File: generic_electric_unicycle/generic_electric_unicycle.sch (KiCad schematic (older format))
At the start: 2 parts

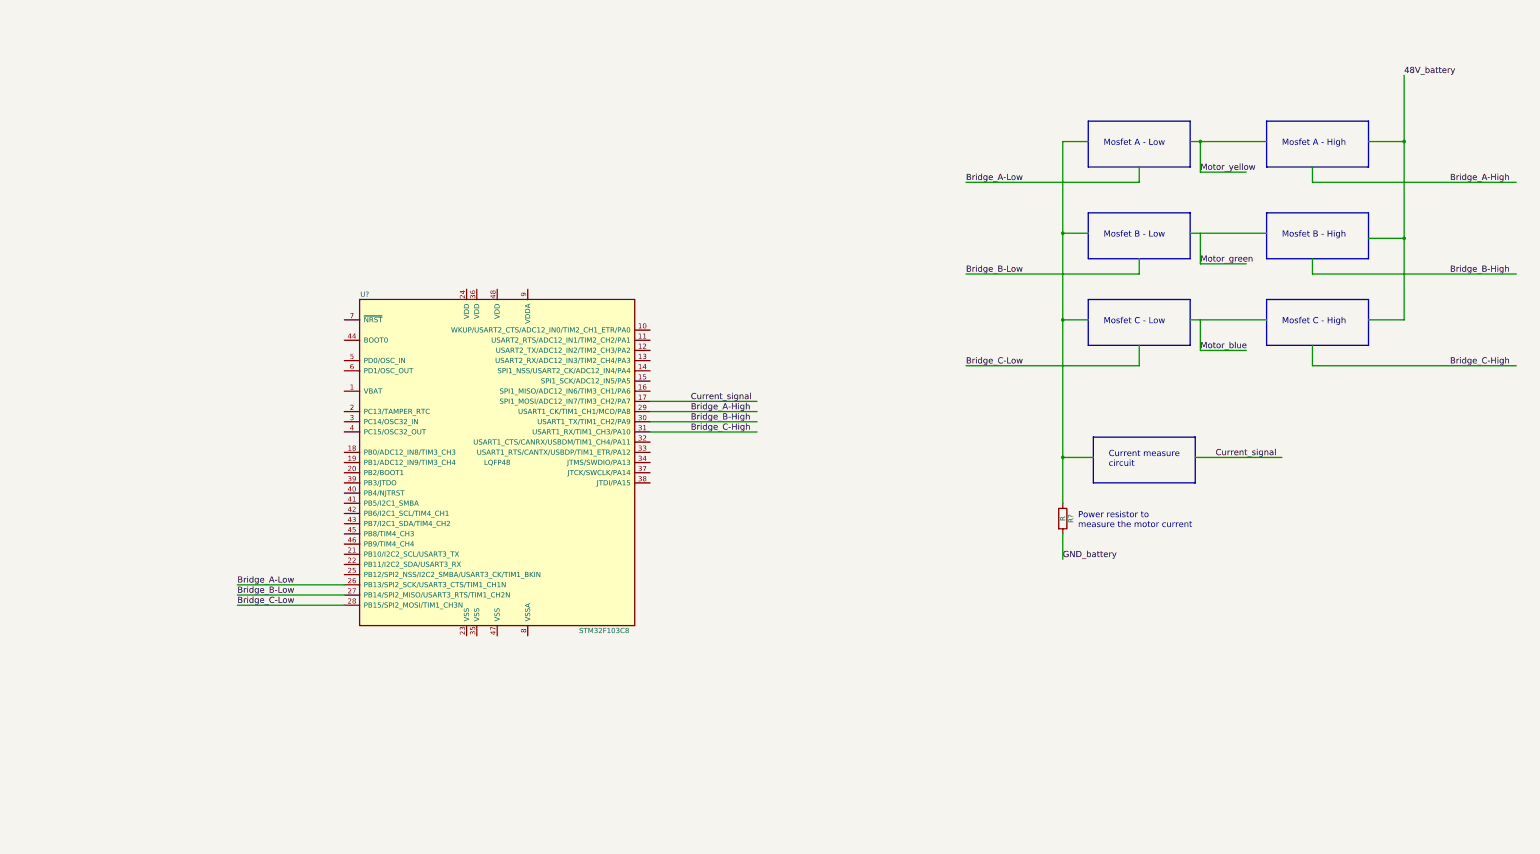
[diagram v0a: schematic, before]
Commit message: Added the hall sensors
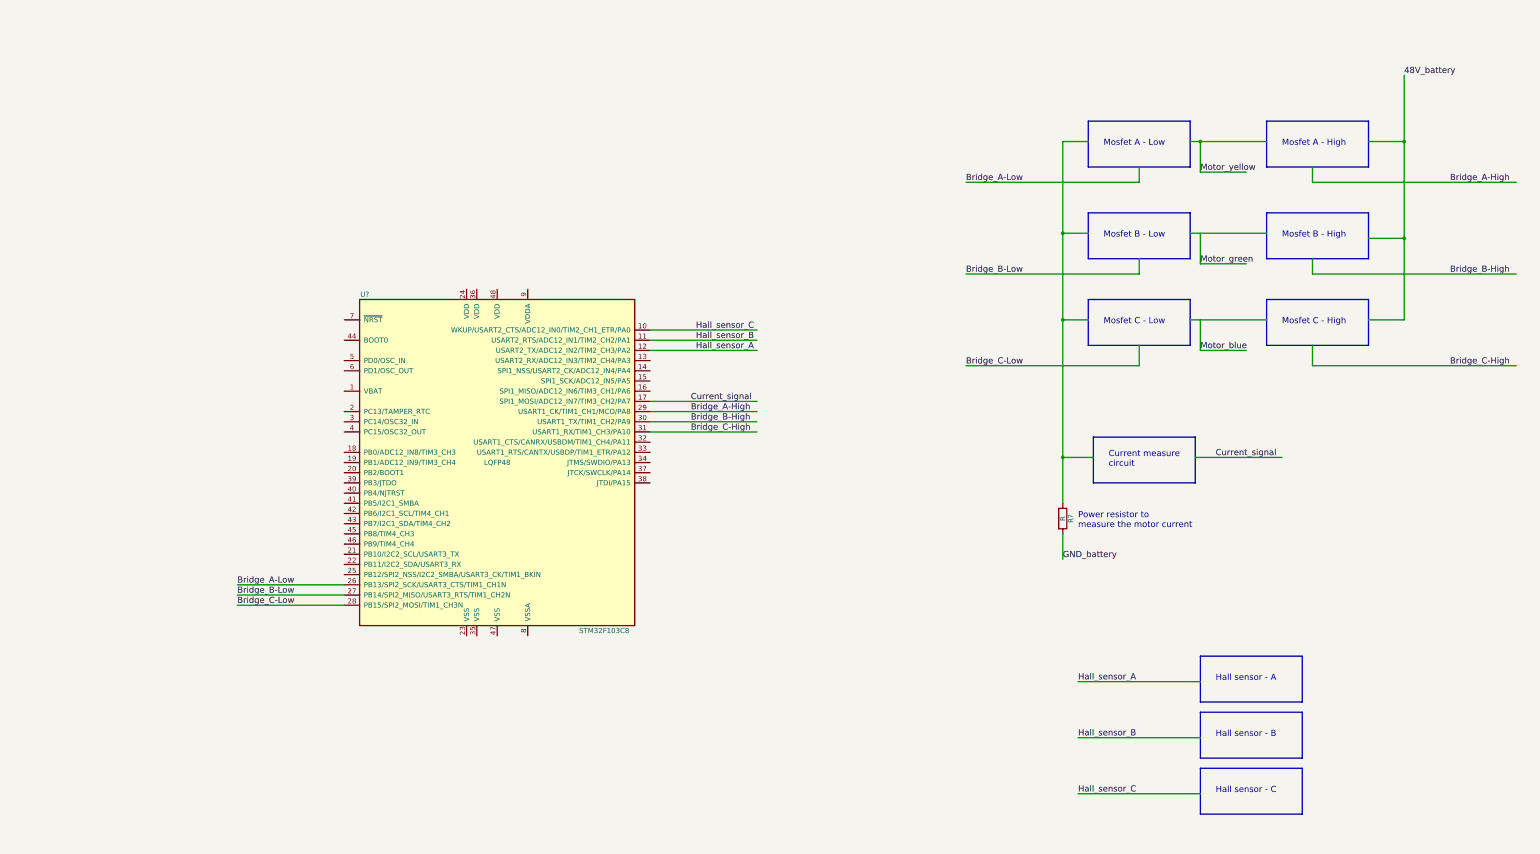
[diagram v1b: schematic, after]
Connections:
- net labels added: Hall_sensor_A, Hall_sensor_B, Hall_sensor_C
- wire segments 39 -> 51
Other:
- note added: "Hall sensor - A"
- note added: "Hall sensor - B"
- note added: "Hall sensor - C"
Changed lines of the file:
@@
 LIBS:valves
 LIBS:stm32
+LIBS:generic_electric_unicycle-cache
 EELAYER 25 0
 EELAYER END
@@
 	14350 2200 14000 2200
 Wire Wire Line
-	14350 1550 14350 3950
+	14350 1550 14350 2200
+Wire Wire Line
+	14350 2200 14350 3150
+Wire Wire Line
+	14350 3150 14350 3950
 Wire Wire Line
 	14350 3150 14000 3150
@@
 	11000 3950 11250 3950
 Wire Wire Line
-	11000 2200 11000 5750
+	11000 2200 11000 3100
+Wire Wire Line
+	11000 3100 11000 3950
+Wire Wire Line
+	11000 3950 11000 5300
+Wire Wire Line
+	11000 5300 11000 5750
 Wire Wire Line
 	11250 2200 11000 2200
@@
 Bridge_C-Low
 Wire Wire Line
-	12250 2200 13000 2200
+	12250 2200 12350 2200
+Wire Wire Line
+	12350 2200 13000 2200
 Wire Wire Line
 	12250 3100 13000 3100
@@
 Wire Wire Line
 	13450 4400 13450 4200
+Wire Bus Line
+	12350 7250 13350 7250
+Wire Bus Line
+	13350 7700 12350 7700
+Wire Bus Line
+	12350 7700 12350 7250
+Text Notes 12500 7500 0    60   ~ 0
+Hall sensor - A
+Wire Wire Line
+	11150 7500 12350 7500
+Text Label 11150 7500 0    60   ~ 0
+Hall_sensor_A
+Wire Bus Line
+	13350 7250 13350 7700
+Wire Bus Line
+	12350 7800 13350 7800
+Wire Bus Line
+	13350 8250 12350 8250
+Wire Bus Line
+	12350 8250 12350 7800
+Text Notes 12500 8050 0    60   ~ 0
+Hall sensor - B
+Wire Wire Line
+	11150 8050 12350 8050
+Text Label 11150 8050 0    60   ~ 0
+Hall_sensor_B
+Wire Bus Line
+	13350 7800 13350 8250
+Wire Bus Line
+	12350 8350 13350 8350
+Wire Bus Line
+	13350 8800 12350 8800
+Wire Bus Line
+	12350 8800 12350 8350
+Text Notes 12500 8600 0    60   ~ 0
+Hall sensor - C
+Wire Wire Line
+	11150 8600 12350 8600
+Text Label 11150 8600 0    60   ~ 0
+Hall_sensor_C
+Wire Bus Line
+	13350 8350 13350 8800
+Wire Wire Line
+	6950 4250 8000 4250
+Text Label 7400 4250 0    60   ~ 0
+Hall_sensor_A
+Wire Wire Line
+	6950 4150 8000 4150
+Text Label 7400 4150 0    60   ~ 0
+Hall_sensor_B
+Wire Wire Line
+	6950 4050 8000 4050
+Text Label 7400 4050 0    60   ~ 0
+Hall_sensor_C
 $EndSCHEMATC

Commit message: Added all the pins connections that we know to the STM32F
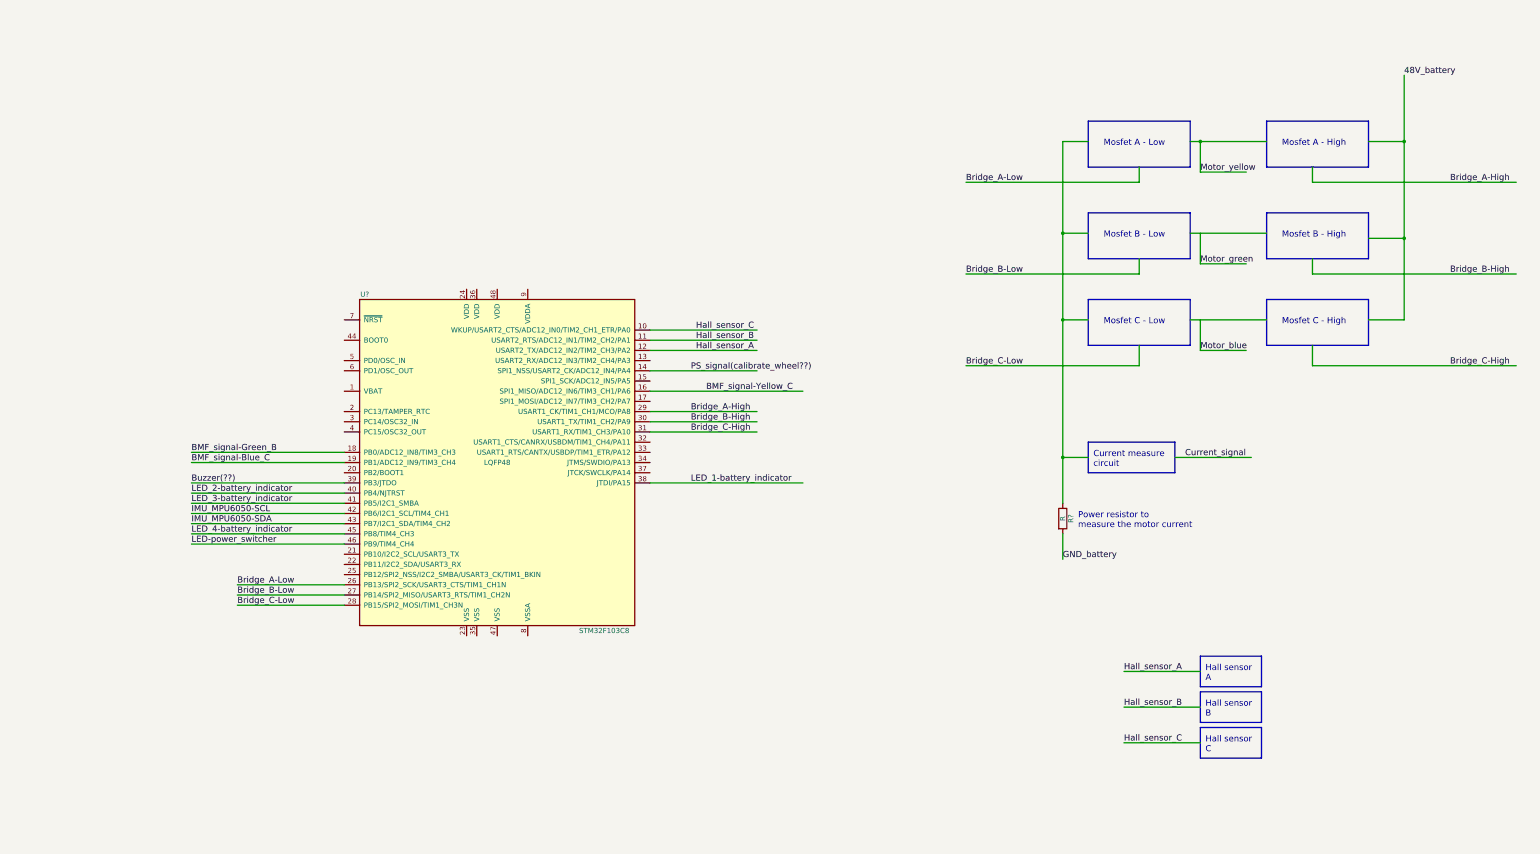
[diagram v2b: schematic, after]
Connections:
- net labels added: BMF_signal-Blue_C, BMF_signal-Green_B, BMF_signal-Yellow_C, Buzzer(??), IMU_MPU6050-SCL, IMU_MPU6050-SDA, LED-power_switcher, LED_1-battery_indicator, LED_2-battery_indicator, LED_3-battery_indicator, LED_4-battery_indicator, PS_signal(calibrate_wheel??)
- wire segments 51 -> 62
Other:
- note added: "Hall sensor\nA"
- note added: "Hall sensor\nB"
- note added: "Hall sensor\nC"
- note removed: "Hall sensor - A"
- note removed: "Hall sensor - B"
- note removed: "Hall sensor - C"
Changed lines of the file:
@@
 	11750 4400 11750 4200
 Wire Bus Line
-	11300 5100 12300 5100
+	11250 5150 12100 5150
 Wire Bus Line
-	12300 5100 12300 5550
+	12100 5150 12100 5450
 Wire Bus Line
-	12300 5550 11300 5550
+	12100 5450 11250 5450
 Wire Bus Line
-	11300 5550 11300 5100
-Text Notes 11450 5400 0    60   ~ 0
+	11250 5450 11250 5150
+Text Notes 11300 5400 0    60   ~ 0
 Current measure\ncircuit
 Wire Wire Line
-	12300 5300 13150 5300
+	12100 5300 12850 5300
 Wire Wire Line
-	11300 5300 11000 5300
+	11250 5300 11000 5300
 Connection ~ 11000 5300
-Text Label 12500 5300 0    60   ~ 0
+Text Label 12200 5300 0    60   ~ 0
 Current_signal
 Wire Wire Line
-	6950 4750 8000 4750
-Text Label 7350 4750 0    60   ~ 0
-Current_signal
+	6950 4450 8000 4450
+Text Label 7350 4450 0    60   ~ 0
+PS_signal(calibrate_wheel??)
 Wire Wire Line
 	13450 2600 15450 2600
@@
 	13450 4400 13450 4200
 Wire Bus Line
-	12350 7250 13350 7250
+	12350 7250 12950 7250
 Wire Bus Line
-	13350 7700 12350 7700
+	12950 7550 12350 7550
 Wire Bus Line
-	12350 7700 12350 7250
-Text Notes 12500 7500 0    60   ~ 0
-Hall sensor - A
+	12350 7550 12350 7250
+Text Notes 12400 7500 0    60   ~ 0
+Hall sensor\nA
 Wire Wire Line
-	11150 7500 12350 7500
-Text Label 11150 7500 0    60   ~ 0
+	11600 7400 12350 7400
+Text Label 11600 7400 0    60   ~ 0
 Hall_sensor_A
 Wire Bus Line
-	13350 7250 13350 7700
-Wire Bus Line
-	12350 7800 13350 7800
-Wire Bus Line
-	13350 8250 12350 8250
-Wire Bus Line
-	12350 8250 12350 7800
-Text Notes 12500 8050 0    60   ~ 0
-Hall sensor - B
-Wire Wire Line
-	11150 8050 12350 8050
-Text Label 11150 8050 0    60   ~ 0
-Hall_sensor_B
-Wire Bus Line
-	13350 7800 13350 8250
-Wire Bus Line
-	12350 8350 13350 8350
-Wire Bus Line
-	13350 8800 12350 8800
-Wire Bus Line
-	12350 8800 12350 8350
-Text Notes 12500 8600 0    60   ~ 0
-Hall sensor - C
-Wire Wire Line
-	11150 8600 12350 8600
-Text Label 11150 8600 0    60   ~ 0
-Hall_sensor_C
-Wire Bus Line
-	13350 8350 13350 8800
+	12950 7250 12950 7550
 Wire Wire Line
 	6950 4250 8000 4250
@@
 Text Label 7400 4050 0    60   ~ 0
 Hall_sensor_C
+Wire Wire Line
+	6950 5550 8450 5550
+Text Label 7350 5550 0    60   ~ 0
+LED_1-battery_indicator
+Wire Wire Line
+	2450 5650 3950 5650
+Text Label 2450 5650 0    60   ~ 0
+LED_2-battery_indicator
+Wire Wire Line
+	2450 5750 3950 5750
+Text Label 2450 5750 0    60   ~ 0
+LED_3-battery_indicator
+Wire Wire Line
+	2450 6050 3950 6050
+Text Label 2450 6050 0    60   ~ 0
+LED_4-battery_indicator
+Wire Wire Line
+	2450 6150 3950 6150
+Text Label 2450 6150 0    60   ~ 0
+LED-power_switcher
+Wire Wire Line
+	2450 5850 3950 5850
+Text Label 2450 5850 0    60   ~ 0
+IMU_MPU6050-SCL
+Wire Wire Line
+	2450 5950 3950 5950
+Text Label 2450 5950 0    60   ~ 0
+IMU_MPU6050-SDA
+Wire Wire Line
+	2450 5550 3950 5550
+Text Label 2450 5550 0    60   ~ 0
+Buzzer(??)
+Wire Bus Line
+	12350 7600 12950 7600
+Wire Bus Line
+	12950 7900 12350 7900
+Wire Bus Line
+	12350 7900 12350 7600
+Text Notes 12400 7850 0    60   ~ 0
+Hall sensor\nB
+Wire Wire Line
+	11600 7750 12350 7750
+Text Label 11600 7750 0    60   ~ 0
+Hall_sensor_B
+Wire Bus Line
+	12950 7600 12950 7900
+Wire Bus Line
+	12350 7950 12950 7950
+Wire Bus Line
+	12950 8250 12350 8250
+Wire Bus Line
+	12350 8250 12350 7950
+Text Notes 12400 8200 0    60   ~ 0
+Hall sensor\nC
+Wire Wire Line
+	11600 8100 12350 8100
+Text Label 11600 8100 0    60   ~ 0
+Hall_sensor_C
+Wire Bus Line
+	12950 7950 12950 8250
+Wire Wire Line
+	2450 5250 3950 5250
+Text Label 2450 5250 0    60   ~ 0
+BMF_signal-Green_B
+Wire Wire Line
+	2450 5350 3950 5350
+Text Label 2450 5350 0    60   ~ 0
+BMF_signal-Blue_C
+Wire Wire Line
+	6950 4650 8450 4650
+Text Label 7500 4650 0    60   ~ 0
+BMF_signal-Yellow_C
 $EndSCHEMATC

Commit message: Small change
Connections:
- net labels added: BMF_signal-Yellow_A
- net labels removed: BMF_signal-Yellow_C
- wire segments 62 -> 63
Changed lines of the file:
@@
 BMF_signal-Blue_C
 Wire Wire Line
-	6950 4650 8450 4650
-Text Label 7500 4650 0    60   ~ 0
-BMF_signal-Yellow_C
+	6950 4650 8000 4650
+Text Label 7350 4650 0    60   ~ 0
+BMF_signal-Yellow_A
+Wire Wire Line
+	6950 4750 8000 4750
+Text Label 7350 4750 0    60   ~ 0
+Current_signal
 $EndSCHEMATC

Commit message: added the schematic for current measure.
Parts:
- added C? (x2): C, symbol C
- added Q?: ??, TO-92, symbol BC547
- added R?: 0.007, symbol R
- added R? (x2): 1k, symbol R
- added R?: 20k, symbol R
- added R?: 510, symbol R
- added R? (x2): 10k, symbol R
- added R?: 220k, symbol R
- added U?: LM358, symbol LM2903
- R?: value R -> 0.007
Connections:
- net labels added: +3V3, GND, Max_current_signal
- wire segments 63 -> 94
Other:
- note removed: "Current measure\ncircuit"
- moved on the sheet: R?

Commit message: Correcton of circuito for current measurement
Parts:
- added C?: C, symbol C
- added Q?: ??, TO-92, symbol BC547
- added R? (x2): 1k5, symbol R
- added R?: 20k, symbol R
- added R?: 510, symbol R
- added R?: 2k2, symbol R
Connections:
- wire segments 94 -> 91
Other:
- moved on the sheet: R?, U?
